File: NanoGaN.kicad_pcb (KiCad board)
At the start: 6 copper layers, 60 x 100 mm, 210 parts, among them J1 XT60-M, J10 Conn_01x06, J11 Conn_01x04, J12 USB4085-GF-A, J14 Conn_01x03, J2 XT60-M, J3 Phase_U, J4 Phase_V, J5 Phase_W, J6 FTSH-107-01-L-DV-K-TR, J7 Conn_01x03, J8 Conn_01x02, J9 Conn_01x07, Q1 IGC025S08S1, Q2 IGC025S08S1, Q3 IGC025S08S1, Q4 IGC025S08S1, Q5 IGC025S08S1, Q6 IGC025S08S1, Q7 Si2302CDS, U1 STM32H723VGTx, U12 LMG1205YFXR, U13 BMI323, U14 AS5047P-ATST, U15 TCAN1044VDRQ1, U19 NCS2220AMUT1G, U2 LMR51635XDDCR, U20 NCS2220AMUT1G, U21 NCS2220AMUT1G, U3 AMS1117, U4 ACS37030LLZATR-065B3, U5 LMG1205YFXR, U6 ACS37030LLZATR-065B3, U7 ACS37030LLZATR-065B3, U8 LMG1205YFXR, X1 8MHz

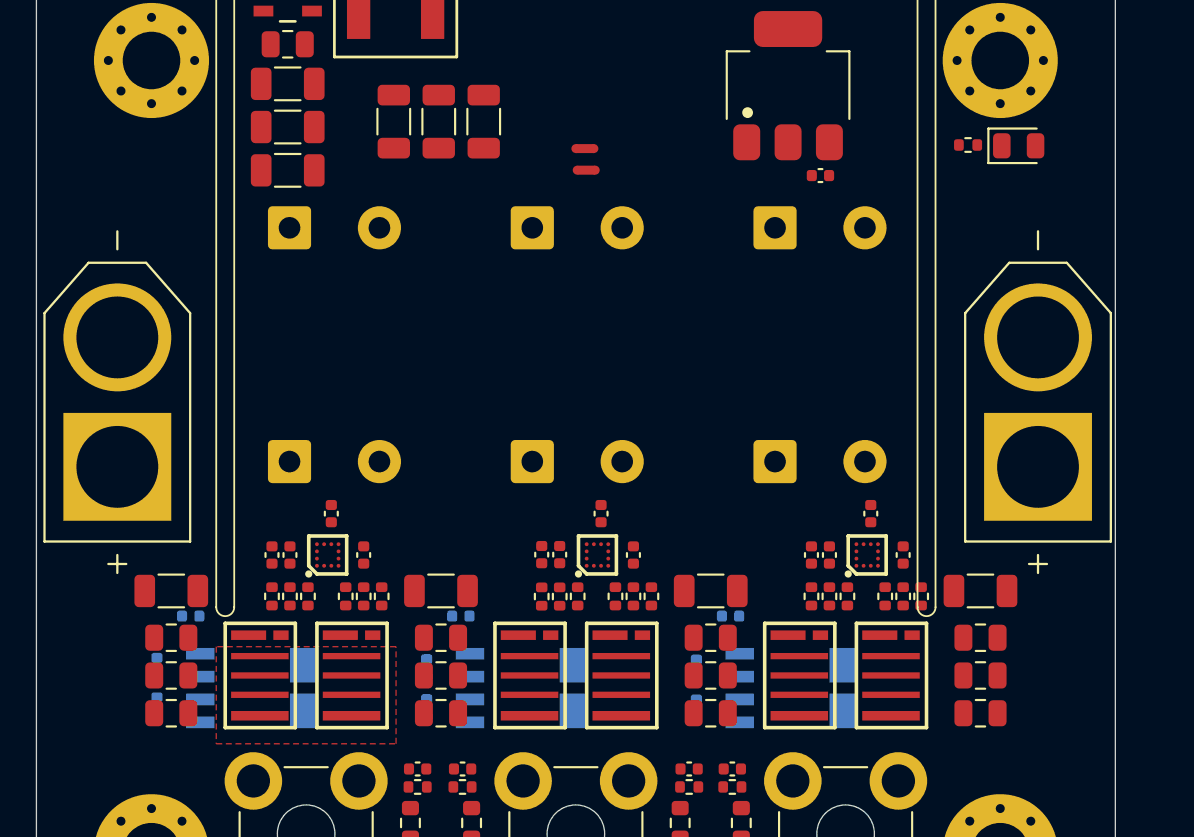
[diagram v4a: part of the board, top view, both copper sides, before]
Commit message: new version of heatsink, channel and mounting holes
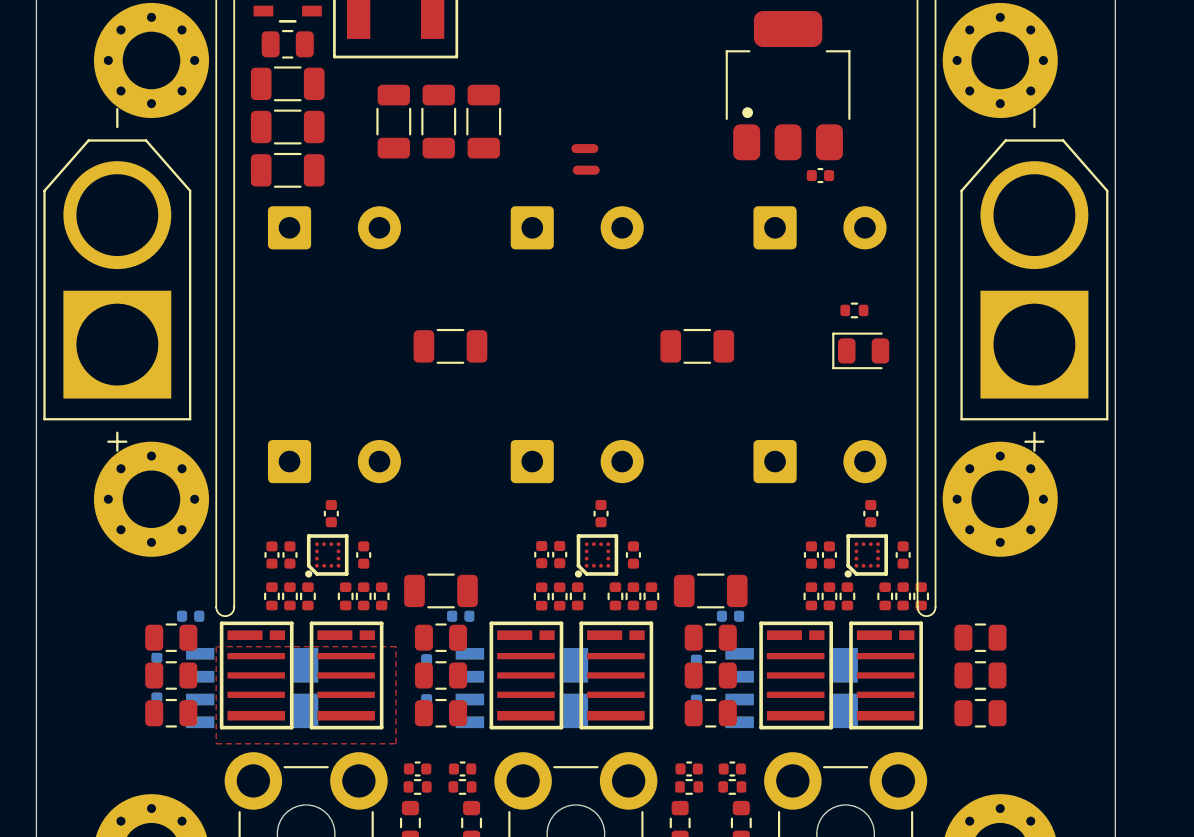
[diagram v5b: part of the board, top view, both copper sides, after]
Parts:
- removed HS2, HS3: Heatsink, NanoGaN:HSB01-080808
- added MH8: M3, MountingHole:MountingHole_3.2mm_M3_Pad_Via, F.Cu at (121.6, 123.0)
- added MH9: M3, MountingHole:MountingHole_3.2mm_M3_Pad_Via, F.Cu at (168.8, 123.0)
- HS1: footprint NanoGaN:HSB01-080808 -> NanoGaN:ICK_S
- moved C68 20.8 mm to (151.9, 114.5)
- moved C46 20.6 mm to (138.2, 114.5)
- moved HS1 15.0 mm to (145.2, 133.0)
- moved D1 14.3 mm to (161.2, 114.8)
- moved R3 11.2 mm to (160.7, 112.5)
- moved J1 6.80 mm to (170.7, 110.8)
- moved J2 6.80 mm to (119.7, 110.8)
- moved Q1 0.30 mm to (162.7, 132.8)
- moved Q3 0.30 mm to (147.7, 132.8)
- moved Q5 0.30 mm to (132.7, 132.8)
- moved Q2 0.20 mm to (157.7, 132.8)
- moved Q4 0.20 mm to (142.7, 132.8)
- moved Q6 0.20 mm to (127.7, 132.8)

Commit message: wip layout (power)
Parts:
- R13, R14, R17, R18, R24, R25: moved to B.Cu
- moved C18 30.0 mm to (151.5, 168.0)
- moved C36 30.0 mm to (138.9, 168.0)
- moved C85 30.0 mm to (136.4, 168.0)
- moved C87 30.0 mm to (153.9, 168.0)
- moved R10 30.0 mm to (154.4, 171.0)
- moved R12 30.0 mm to (153.9, 169.0)
- moved R19 30.0 mm to (139.4, 171.0)
- moved R20 30.0 mm to (138.9, 169.0)
- moved R26 30.0 mm to (136.0, 171.0)
- moved R27 30.0 mm to (136.4, 169.0)
- moved R4 30.0 mm to (151.0, 171.0)
- moved R5 30.0 mm to (151.5, 169.0)
- moved C68 27.3 mm to (167.1, 137.2)
- moved C46 27.2 mm to (123.3, 137.2)
- moved C17 10.9 mm to (138.1, 139.0), turned to -90 degrees
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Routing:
- net /HalfBridgeV/PHASE: vias 0 -> 9
- net /HalfBridgeV/HS: vias 0 -> 30
- added copper zone on In1.Cu, net +5V
- added copper zone on In2.Cu, net +5V
- added copper zone on In3.Cu, net +5V
- added copper zone on In4.Cu, net +5V
- added copper zone on B.Cu, net /HalfBridgeV/HS
- added copper zone on F.Cu, net /HalfBridgeV/HS
- added copper zone on In1.Cu, net /HalfBridgeV/HS
- added copper zone on In2.Cu, net /HalfBridgeV/HS
- added copper zone on In3.Cu, net /HalfBridgeV/HS
- added copper zone on In4.Cu, net /HalfBridgeV/HS
- added copper zone on B.Cu, net /HalfBridgeV/PHASE
- added copper zone on F.Cu, net /HalfBridgeV/PHASE
- added copper zone on In1.Cu, net /HalfBridgeV/PHASE
- added copper zone on In2.Cu, net /HalfBridgeV/PHASE
- added copper zone on In3.Cu, net /HalfBridgeV/PHASE
- added copper zone on In4.Cu, net /HalfBridgeV/PHASE
- added copper zone on F.Cu, net PGND
- added copper zone on In4.Cu, net PGND
- added copper zone on F.Cu, net U_DC
- added copper zone on In3.Cu, net U_DC
- removed copper zone on F.Cu, net /HalfBridgeW/HS

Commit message: wip layout
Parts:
- removed C100, C101, C92: 100n, Capacitor_SMD:C_0402_1005Metric
- removed C79, C93: 1u, Capacitor_SMD:C_0402_1005Metric
- removed C94, C95: 1n, Capacitor_SMD:C_0201_0603Metric
- removed NT1, NT2: NetTie_2, NetTie:NetTie-2_SMD_Pad0.5mm
- removed R63, R64, R65, R66, R67, R68: 10k, Resistor_SMD:R_0402_1005Metric
- removed R69, R70, R71, R72, R73, R74: 39k, Resistor_SMD:R_0603_1608Metric
- removed U19, U20, U21: NCS2220AMUT1G, NanoGaN:UDFN8_1P6X1P6_ONS
- C18, C24, C25, C26, C28, C33, C36, C38, C39, C58, C59, C85, C87, C89, C91: footprint Capacitor_SMD:C_0402_1005Metric -> Capacitor_SMD:C_0603_1608Metric_Pad1.08x0.95mm_HandSolder
- J12: value USB4085-GF-A -> USB_C_Receptacle_USB2.0_16P; footprint Connector_USB:USB_C_Receptacle_GCT_USB4085 -> Connector_USB:USB_C_Receptacle_GCT_USB4105-xx-A_16P_TopMnt_Horizontal
- moved HS1 114.2 mm to (259.4, 133.0)
- moved CC1 72.8 mm to (217.9, 77.5)
- moved D1 64.0 mm to (150.4, 51.7), turned to 90 degrees
- moved R3 58.7 mm to (150.4, 54.7), turned to 90 degrees
- moved C36 55.9 mm to (132.8, 112.4)
- moved C85 55.9 mm to (130.3, 112.4)
- moved R19 55.9 mm to (133.3, 115.4)
- moved R20 55.9 mm to (132.8, 113.4)
- moved R26 55.9 mm to (129.9, 115.4)
- moved R27 55.9 mm to (130.3, 113.4)
- moved C18 55.8 mm to (155.3, 112.3)
- moved C87 55.8 mm to (157.7, 112.3)
- moved R10 55.8 mm to (158.2, 115.3)
- moved R12 55.8 mm to (157.7, 113.3)
- moved R4 55.8 mm to (154.8, 115.3)
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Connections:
- C1 pad 2: PGND -> GND
- C10 pad 2: AGND -> GND
- C11 pad 2: PGND -> GND
- C12 pad 2: PGND -> GND
- C13 pad 2: PGND -> GND
- C14 pad 2: PGND -> GND
- C15 pad 2: PGND -> GND
- C16 pad 2: PGND -> GND
- C17 pad 2: PGND -> GND
- C18 pad 2: PGND -> GND
- C2 pad 2: PGND -> GND
- C20 pad 2: PGND -> GND
- C22 pad 2: PGND -> GND
- C23 pad 2: PGND -> GND
- C24 pad 2: PGND -> GND
- C25 pad 2: PGND -> GND
- C26 pad 2: PGND -> GND
- C27 pad 2: PGND -> GND
- C28 pad 2: PGND -> GND
- C29 pad 2: PGND -> GND
- C3 pad 2: PGND -> GND
- C30 pad 2: PGND -> GND
- C31 pad 2: PGND -> GND
- C32 pad 2: PGND -> GND
- C33 pad 2: PGND -> GND
- C35 pad 2: PGND -> GND
- C36 pad 2: PGND -> GND
- C38 pad 2: PGND -> GND
- C39 pad 2: PGND -> GND
- C4 pad 2: PGND -> GND
- C41 pad 2: PGND -> GND
- C42 pad 2: PGND -> GND
- C43 pad 2: PGND -> GND
- C44 pad 2: PGND -> GND
- C45 pad 2: PGND -> GND
- C46 pad 2: PGND -> GND
- C47 pad 2: PGND -> GND
- C48 pad 2: PGND -> GND
- C49 pad 2: PGND -> GND
- C50 pad 2: PGND -> GND
- C6 pad 2: PGND -> GND
- C67 pad 2: PGND -> GND
- C68 pad 2: PGND -> GND
- C7 pad 2: PGND -> GND
- C72 pad 2: AGND -> GND
- C80 pad 2: AGND -> GND
- C81 pad 2: PGND -> GND
- C82 pad 2: PGND -> GND
- C85 pad 2: PGND -> GND
- C86 pad 2: PGND -> GND
- C87 pad 2: PGND -> GND
- C88 pad 2: PGND -> GND
- C89 pad 2: PGND -> GND
- C9 pad 2: AGND -> GND
- C90 pad 2: PGND -> GND
- C91 pad 2: PGND -> GND
- J1 pad N: PGND -> GND
- J2 pad N: PGND -> GND
- MH4 pad 1: PGND -> GND
- MH5 pad 1: PGND -> GND
- MH6 pad 1: PGND -> GND
- MH7 pad 1: PGND -> GND
- MH8 pad 1: PGND -> GND
- MH9 pad 1: PGND -> GND
- Q2 pad 3: PGND -> GND
- Q2 pad 5: PGND -> GND
- Q2 pad 6: PGND -> GND
- Q4 pad 3: PGND -> GND
- Q4 pad 5: PGND -> GND
- Q4 pad 6: PGND -> GND
- Q6 pad 3: PGND -> GND
- Q6 pad 5: PGND -> GND
- Q6 pad 6: PGND -> GND
- R12 pad 2: PGND -> GND
- R14 pad 2: PGND -> GND
- R18 pad 2: PGND -> GND
- R2 pad 2: PGND -> GND
- R20 pad 2: PGND -> GND
- R25 pad 2: PGND -> GND
- R27 pad 2: PGND -> GND
- R5 pad 2: PGND -> GND
- U1 pad 19: AGND -> GND
- U1 pad 38: /HalfBridgeU/LI -> /HalfBridgeW/LI
- U1 pad 39: /HalfBridgeU/HI -> /HalfBridgeW/HI
- U1 pad 42: /HalfBridgeW/LI -> /HalfBridgeU/LI
- U1 pad 43: /HalfBridgeW/HI -> /HalfBridgeU/HI
- U12 pad A2: PGND -> GND
- U2 pad 4: PGND -> GND
- U4 pad 3: PGND -> GND
- U5 pad A2: PGND -> GND
- U6 pad 3: PGND -> GND
- U7 pad 3: PGND -> GND
- U8 pad A2: PGND -> GND
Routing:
- net /MCU/HSE_OUT: track 0.00 -> 0.52 mm
- net GND: vias 0 -> 9
- net /HalfBridgeW/PHASE: vias 0 -> 9
- net /HalfBridgeW/HS: vias 0 -> 30
- net /HalfBridgeV/LOW_GATE: vias 0 -> 1
- net /HalfBridgeV/HIGH_GATE: vias 0 -> 1
- net /HalfBridgeU/PHASE: vias 0 -> 9
- net /HalfBridgeU/HS: vias 0 -> 30
- net +5V: vias 0 -> 3
- net +3V3: vias 0 -> 3
- added copper zone on In2.Cu, net +3V3
- added copper zone on B.Cu, net /HalfBridgeU/HS
- added copper zone on F.Cu, net /HalfBridgeU/HS
- added copper zone on In1.Cu, net /HalfBridgeU/HS
- added copper zone on In2.Cu, net /HalfBridgeU/HS
- added copper zone on In3.Cu, net /HalfBridgeU/HS
- added copper zone on In4.Cu, net /HalfBridgeU/HS
- added copper zone on B.Cu, net /HalfBridgeU/PHASE
- added copper zone on F.Cu, net /HalfBridgeU/PHASE
- added copper zone on In1.Cu, net /HalfBridgeU/PHASE
- added copper zone on In2.Cu, net /HalfBridgeU/PHASE
- added copper zone on In3.Cu, net /HalfBridgeU/PHASE
- added copper zone on In4.Cu, net /HalfBridgeU/PHASE
- added copper zone on F.Cu, net /HalfBridgeV/HIGH_GATE
- added copper zone on F.Cu, net /HalfBridgeV/LOW_GATE
- added copper zone on B.Cu, net /HalfBridgeW/HS
- added copper zone on F.Cu, net /HalfBridgeW/HS
- added copper zone on In1.Cu, net /HalfBridgeW/HS
- added copper zone on In2.Cu, net /HalfBridgeW/HS
- added copper zone on In3.Cu, net /HalfBridgeW/HS
- added copper zone on In4.Cu, net /HalfBridgeW/HS
- added copper zone on B.Cu, net /HalfBridgeW/PHASE
- added copper zone on F.Cu, net /HalfBridgeW/PHASE
- added copper zone on In1.Cu, net /HalfBridgeW/PHASE
- added copper zone on In2.Cu, net /HalfBridgeW/PHASE
- added copper zone on In3.Cu, net /HalfBridgeW/PHASE
- added copper zone on In4.Cu, net /HalfBridgeW/PHASE
- added copper zone on In1.Cu, net GND
- added copper zone on In4.Cu, net GND
- added copper zone on B.Cu, net U_DC
- removed copper zone on In1.Cu, net +5V
- removed copper zone on In2.Cu, net +5V
- removed copper zone on In4.Cu, net +5V
- removed copper zone on F.Cu, net PGND
- removed copper zone on In1.Cu, net PGND
- removed copper zone on In4.Cu, net PGND
- removed copper zone on In3.Cu, net U_DC

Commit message: wip layout
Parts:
- added C79: 4u7, Capacitor_SMD:C_0402_1005Metric, F.Cu at (142.3, 87.2)
- added U_HB_PAD: HB_PAD, NanoGaN:HB_PAD, F.Cu at (159.4, 129.1)
- added V_HB_PAD: HB_PAD, NanoGaN:HB_PAD, F.Cu at (131.0, 129.1)
- added V_HB_PAD: HB_PAD, NanoGaN:HB_PAD, F.Cu at (145.2, 129.1)
- moved CC1 27.4 mm to (245.2, 75.0)
- moved C7 14.1 mm to (142.3, 88.2), turned to 0 degrees
- moved U3 6.32 mm to (136.2, 90.0), turned to 180 degrees
- moved C52 5.30 mm to (121.8, 83.6)
- moved C64 4.61 mm to (150.7, 60.5), turned to 90 degrees
- moved R42 4.52 mm to (127.6, 83.6), turned to 180 degrees
- moved R43 4.25 mm to (127.6, 84.6), turned to 0 degrees
- moved C8 3.60 mm to (129.9, 91.0), turned to 180 degrees
- moved C63 3.53 mm to (149.7, 60.5), turned to 90 degrees
- moved R11 3.40 mm to (120.8, 83.6), turned to -90 degrees
- moved C37 2.82 mm to (129.9, 90.0), turned to 180 degrees
- moved C40 2.64 mm to (129.9, 89.0), turned to 180 degrees
- moved Q7 2.02 mm to (124.9, 85.6)
- moved R21 1.80 mm to (120.8, 80.1), turned to 90 degrees
- moved C6 1.38 mm to (155.7, 90.5)
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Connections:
- net /HalfBridgeU/HI renamed /HalfBridgeU/GATE+
- net /HalfBridgeU/LI renamed /HalfBridgeU/GATE-
- net /HalfBridgeV/HI renamed /HalfBridgeV/GATE+
- net /HalfBridgeV/LI renamed /HalfBridgeV/GATE-
- net /HalfBridgeW/HI renamed /HalfBridgeW/GATE+
- net /HalfBridgeW/LI renamed /HalfBridgeW/GATE-
- C72 pad 2: GND -> AGND
- C80 pad 2: GND -> AGND
- U1 pad 19: GND -> AGND
- U1 pad 81: /MCU/UART4_RX -> /Connectors/VCP_TX
- U1 pad 82: /MCU/UART4_TX -> /Connectors/VCP_RX
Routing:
- net /Power/SW_SMPS: track 0.00 -> 4.78 mm
- net /Power/SW_FB: track 0.00 -> 2.78 mm
- net /Power/SW_CB: track 0.00 -> 1.39 mm
- net GND: track 0.00 -> 0.89 mm, vias 9 -> 45
- net +5V: track 0.00 -> 0.89 mm, vias 3 -> 19
- net /HalfBridgeW/PHASE: vias 9 -> 0
- net /HalfBridgeW/HS: vias 30 -> 0
- net /HalfBridgeV/PHASE: vias 9 -> 0
- net /HalfBridgeV/HS: vias 30 -> 0
- net /HalfBridgeU/PHASE: vias 9 -> 0
- net /HalfBridgeU/HS: vias 30 -> 0
- net +3V3: vias 3 -> 16
- added copper zone on F.Cu, net +3V3
- added copper zone on F.Cu, net +5V
- added copper zone on F.Cu, net /Power/SW_SMPS
- added copper zone on F.Cu, net GND
